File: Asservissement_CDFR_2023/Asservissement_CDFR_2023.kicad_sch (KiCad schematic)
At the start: 127 parts, among them IC1 A3930KJPTR-T, IC2 A3930KJPTR-T, J1 Connecteur batterie, J10 Free Connecteur, J11 Conn_01x02, J12 Conn_01x02, J13 Connecteur Odométrie, J2 Conn_01x03, J3 Conn_01x05, J4 Connecteur Programmation, J5 Conn_01x03, J6 Connecteur Odométrie, J7 Conn_01x03, J8 Conn_01x03, J9 Conn_01x05, Q1 QM6006D, Q10 QM6006D, Q11 QM6006D, Q12 QM6006D, Q13 Q_NMOS_GDS, Q2 QM6006D, Q3 QM6006D, Q4 QM6006D, Q5 QM6006D, Q6 QM6006D, Q7 QM6006D, Q8 QM6006D, Q9 QM6006D, U1 LM317_SOT-223, U3 STM32F401RCTx, U4 LMR16020PDDA, Y1 Crystal_GND24

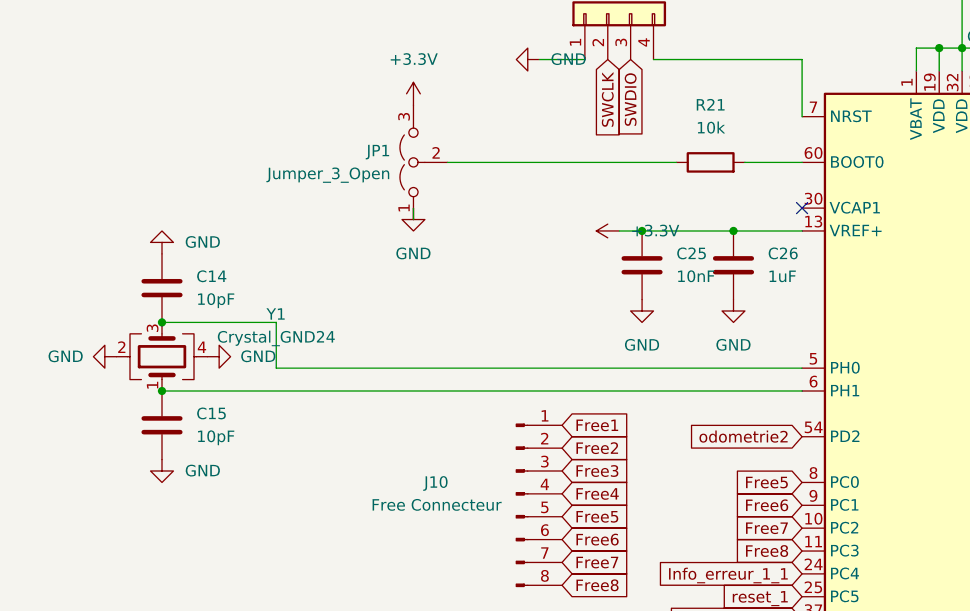
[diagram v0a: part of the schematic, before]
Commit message: add resistor for the crystal, add capacitor to Vcap, add logo and text for the voltage tolerance
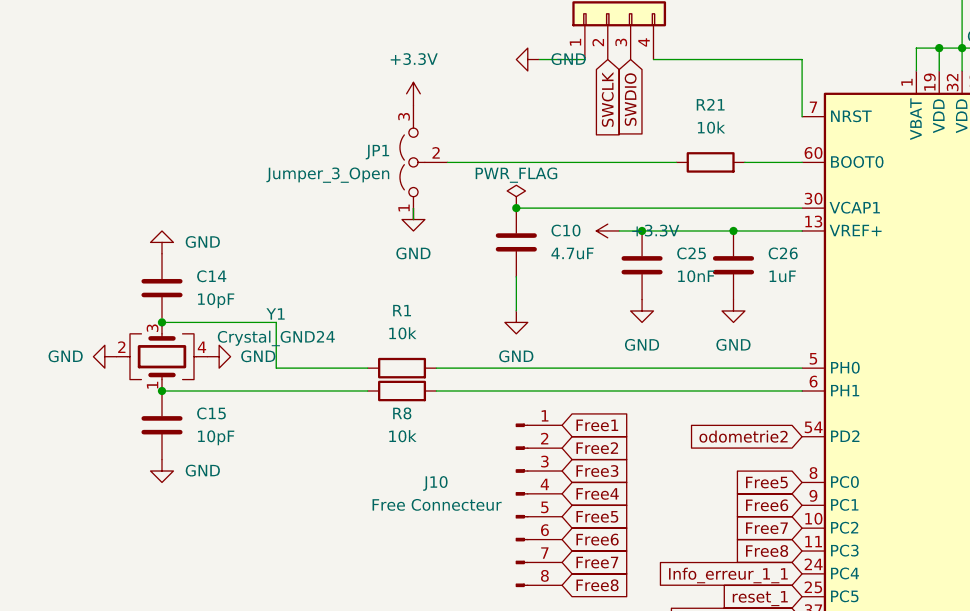
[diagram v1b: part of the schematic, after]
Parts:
- added C10: 4.7uF, Capacitor_SMD:C_0805_2012Metric_Pad1.18x1.45mm_HandSolder, symbol Device:C
- added R1, R8: 10k, Resistor_SMD:R_0805_2012Metric_Pad1.20x1.40mm_HandSolder, symbol Device:R
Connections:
- net GND: now also C10.2
- net at C14.2, Y1.3: now also R1.1; no longer U3.5 (PH0)
- net at U3.30 (VCAP1): now also C10.1
- net at C15.1, Y1.1: now also R8.1; no longer U3.6 (PH1)
- new net: R1.2, U3.5 (PH0)
- new net: R8.2, U3.6 (PH1)
- no-connect marks 14 -> 13
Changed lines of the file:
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@@
   (junction (at 506.73 44.45) (diameter 0) (color 0 0 0 0)
   )
+  (junction (at 92.71 200.66) (diameter 0) (color 0 0 0 0)
+  )
   (junction (at 436.88 92.71) (diameter 0) (color 0 0 0 0)
   )
@@
   (no_connect (at 398.78 241.3))
   (no_connect (at 401.32 241.3))
-  (no_connect (at 124.46 200.66))
   (no_connect (at 388.62 259.08))
   (wire (pts (xy 506.73 69.85) (xy 506.73 82.55))
@@
     (stroke (width 0) (type default) (color 0 0 0 0))
   )
-  (wire (pts (xy 124.46 220.98) (xy 53.34 220.98))
+  (wire (pts (xy 124.46 220.98) (xy 83.82 220.98))
     (stroke (width 0) (type default) (color 0 0 0 0))
   )
@@
     (stroke (width 0) (type default) (color 0 0 0 0))
   )
-  (wire (pts (xy 66.04 218.44) (xy 124.46 218.44))
+  (wire (pts (xy 66.04 218.44) (xy 76.2 218.44))
     (stroke (width 0) (type default) (color 0 0 0 0))
   )
@@
     (stroke (width 0) (type default) (color 0 0 0 0))
   )
+  (wire (pts (xy 92.71 208.28) (xy 92.71 212.09))
+    (stroke (width 0) (type default) (color 0 0 0 0))
+  )
   (wire (pts (xy 53.34 213.36) (xy 66.04 213.36))
     (stroke (width 0) (type default) (color 0 0 0 0))
@@
     (stroke (width 0) (type default) (color 0 0 0 0))
   )
+  (wire (pts (xy 83.82 218.44) (xy 124.46 218.44))
+    (stroke (width 0) (type default) (color 0 0 0 0))
+  )
   (wire (pts (xy 544.83 110.49) (xy 544.83 107.95))
     (stroke (width 0) (type default) (color 0 0 0 0))
@@
     (stroke (width 0) (type default) (color 0 0 0 0))
   )
+  (wire (pts (xy 76.2 220.98) (xy 53.34 220.98))
+    (stroke (width 0) (type default) (color 0 0 0 0))
+  )
   (wire (pts (xy 434.34 284.48) (xy 453.39 284.48))
     (stroke (width 0) (type default) (color 0 0 0 0))
@@
     (stroke (width 0) (type default) (color 0 0 0 0))
   )
+  (wire (pts (xy 92.71 200.66) (xy 124.46 200.66))
+    (stroke (width 0) (type default) (color 0 0 0 0))
+  )
   (wire (pts (xy 147.32 52.07) (xy 147.32 64.77))
     (stroke (width 0) (type default) (color 0 0 0 0))
@@
     (pin "3")
   )
+  (symbol (lib_id "Device:R") (at 80.01 220.98 90) (unit 1)
+    (in_bom yes) (on_board yes)
+    (property "Reference" "R8" (id 0) (at 80.01 223.52 90))
+    (property "Value" "10k" (id 1) (at 80.01 226.06 90))
+    (property "Footprint" "Resistor_SMD:R_0805_2012Metric_Pad1.20x1.40mm_HandSolder" (id 2) (at 80.01 222.758 90)
+      (effects (font (size 1.27 1.27)) hide)
+    )
+    (property "Datasheet" "~" (id 3) (at 80.01 220.98 0)
+      (effects (font (size 1.27 1.27)) hide)
+    )
+    (pin "1")
+    (pin "2")
+  )
   (symbol (lib_id "power:GND") (at 58.42 217.17 90) (unit 1)
     (in_bom yes) (on_board yes)
@@
     (pin "2")
   )
+  (symbol (lib_id "power:GND") (at 92.71 212.09 0) (unit 1)
+    (in_bom yes) (on_board yes) (fields_autoplaced)
+    (property "Reference" "#PWR0109" (id 0) (at 92.71 218.44 0)
+      (effects (font (size 1.27 1.27)) hide)
+    )
+    (property "Value" "GND" (id 1) (at 92.71 217.17 0))
+    (property "Footprint" "" (id 2) (at 92.71 212.09 0)
+      (effects (font (size 1.27 1.27)) hide)
+    )
+    (property "Datasheet" "" (id 3) (at 92.71 212.09 0)
+      (effects (font (size 1.27 1.27)) hide)
+    )
+    (pin "1")
+  )
   (symbol (lib_id "power:GND") (at 196.85 228.6 90) (unit 1)
     (in_bom yes) (on_board yes) (fields_autoplaced)
@@
     (pin "2")
   )
+  (symbol (lib_id "Device:C") (at 92.71 204.47 0) (unit 1)
+    (in_bom yes) (on_board yes) (fields_autoplaced)
+    (property "Reference" "C10" (id 0) (at 96.52 203.1999 0)
+      (effects (font (size 1.27 1.27)) (justify left))
+    )
+    (property "Value" "4.7uF" (id 1) (at 96.52 205.7399 0)
+      (effects (font (size 1.27 1.27)) (justify left))
+    )
+    (property "Footprint" "Capacitor_SMD:C_0805_2012Metric_Pad1.18x1.45mm_HandSolder" (id 2) (at 93.6752 208.28 0)
+      (effects (font (size 1.27 1.27)) hide)
+    )
+    (property "Datasheet" "~" (id 3) (at 92.71 204.47 0)
+      (effects (font (size 1.27 1.27)) hide)
+    )
+    (pin "1")
+    (pin "2")
+  )
   (symbol (lib_id "power:+3.3V") (at 142.24 161.29 0) (unit 1)
     (in_bom yes) (on_board yes) (fields_autoplaced)
@@
     (pin "1")
   )
+  (symbol (lib_id "Device:R") (at 80.01 218.44 90) (unit 1)
+    (in_bom yes) (on_board yes) (fields_autoplaced)
+    (property "Reference" "R1" (id 0) (at 80.01 212.09 90))
+    (property "Value" "10k" (id 1) (at 80.01 214.63 90))
+    (property "Footprint" "Resistor_SMD:R_0805_2012Metric_Pad1.20x1.40mm_HandSolder" (id 2) (at 80.01 220.218 90)
+      (effects (font (size 1.27 1.27)) hide)
+    )
+    (property "Datasheet" "~" (id 3) (at 80.01 218.44 0)
+      (effects (font (size 1.27 1.27)) hide)
+    )
+    (pin "1")
+    (pin "2")
+  )
   (symbol (lib_id "power:GND") (at 408.94 143.51 0) (unit 1)
     (in_bom yes) (on_board yes) (fields_autoplaced)
@@
     (pin "1")
   )
+  (symbol (lib_id "power:PWR_FLAG") (at 92.71 200.66 0) (unit 1)
+    (in_bom yes) (on_board yes)
+    (property "Reference" "#FLG0102" (id 0) (at 92.71 198.755 0)
+      (effects (font (size 1.27 1.27)) hide)
+    )
+    (property "Value" "PWR_FLAG" (id 1) (at 92.71 196.85 0))
+    (property "Footprint" "" (id 2) (at 92.71 200.66 0)
+      (effects (font (size 1.27 1.27)) hide)
+    )
+    (property "Datasheet" "~" (id 3) (at 92.71 200.66 0)
+      (effects (font (size 1.27 1.27)) hide)
+    )
+    (pin "1")
+  )
   (symbol (lib_id "Device:R") (at 468.63 121.92 0) (unit 1)
     (in_bom yes) (on_board yes)
@@
       (reference "#FLG0101") (unit 1) (value "PWR_FLAG") (footprint "")
     )
+    (path "/d5fc98bd-8b4a-41f7-8f4d-cab165222fda"
+      (reference "#FLG0102") (unit 1) (value "PWR_FLAG") (footprint "")
+    )
     (path "/c2ed825f-7bd1-4467-a5ef-8700f9ccf66f"
       (reference "#FLG0104") (unit 1) (value "PWR_FLAG") (footprint "")
@@
       (reference "#PWR0108") (unit 1) (value "+5V") (footprint "")
     )
+    (path "/9d1bcaca-cd1d-4150-9486-f84ed021b7ad"
+      (reference "#PWR0109") (unit 1) (value "GND") (footprint "")
+    )
     (path "/cb70175c-97c6-48d6-a02b-93d4e11b3d49"
       (reference "C1") (unit 1) (value "470nF") (footprint "Capacitor_SMD:C_0805_2012Metric_Pad1.18x1.45mm_HandSolder")
@@
       (reference "C9") (unit 1) (value "47nF") (footprint "Capacitor_SMD:C_0805_2012Metric_Pad1.18x1.45mm_HandSolder")
     )
+    (path "/aa656297-d170-45c0-9433-050e813c7e2b"
+      (reference "C10") (unit 1) (value "4.7uF") (footprint "Capacitor_SMD:C_0805_2012Metric_Pad1.18x1.45mm_HandSolder")
+    )
     (path "/3229e465-658c-497b-aa13-bb46a30754bf"
       (reference "C11") (unit 1) (value "100uF") (footprint "Capacitor_SMD:CP_Elec_10x10.5")
@@
       (reference "Q13") (unit 1) (value "Q_NMOS_GDS") (footprint "Package_TO_SOT_SMD:TO-252-2")
     )
+    (path "/bf57164e-1c8b-4348-9c0e-1bd3168f94fd"
+      (reference "R1") (unit 1) (value "10k") (footprint "Resistor_SMD:R_0805_2012Metric_Pad1.20x1.40mm_HandSolder")
+    )
     (path "/cf693dd7-8b45-433c-b7b1-3d9bff0f41a1"
       (reference "R2") (unit 1) (value "2k4") (footprint "Resistor_SMD:R_0805_2012Metric_Pad1.20x1.40mm_HandSolder")
@@
       (reference "R7") (unit 1) (value "560") (footprint "Resistor_SMD:R_0805_2012Metric_Pad1.20x1.40mm_HandSolder")
     )
+    (path "/56846ada-828b-42f8-a2c3-f017ddfc46d7"
+      (reference "R8") (unit 1) (value "10k") (footprint "Resistor_SMD:R_0805_2012Metric_Pad1.20x1.40mm_HandSolder")
+    )
     (path "/5cb72c38-3e9e-44d9-be58-abf36ec7a07c"

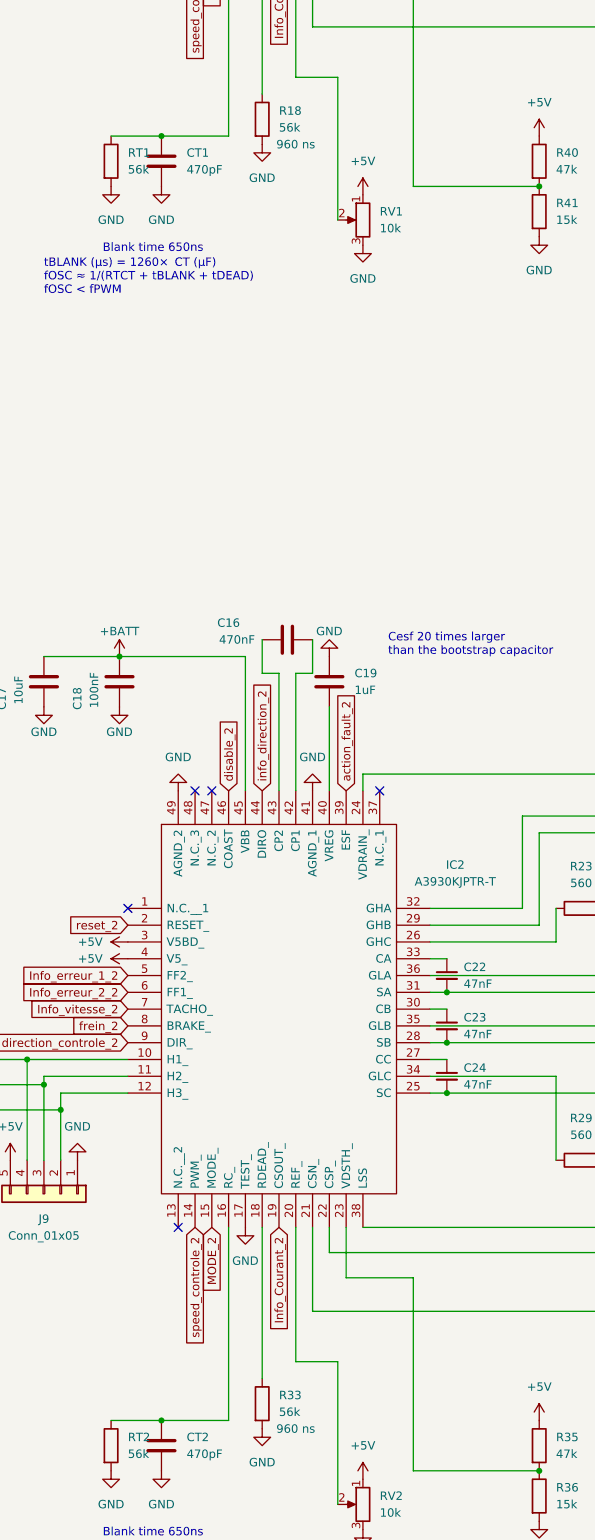
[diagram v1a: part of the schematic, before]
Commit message: change one resistor
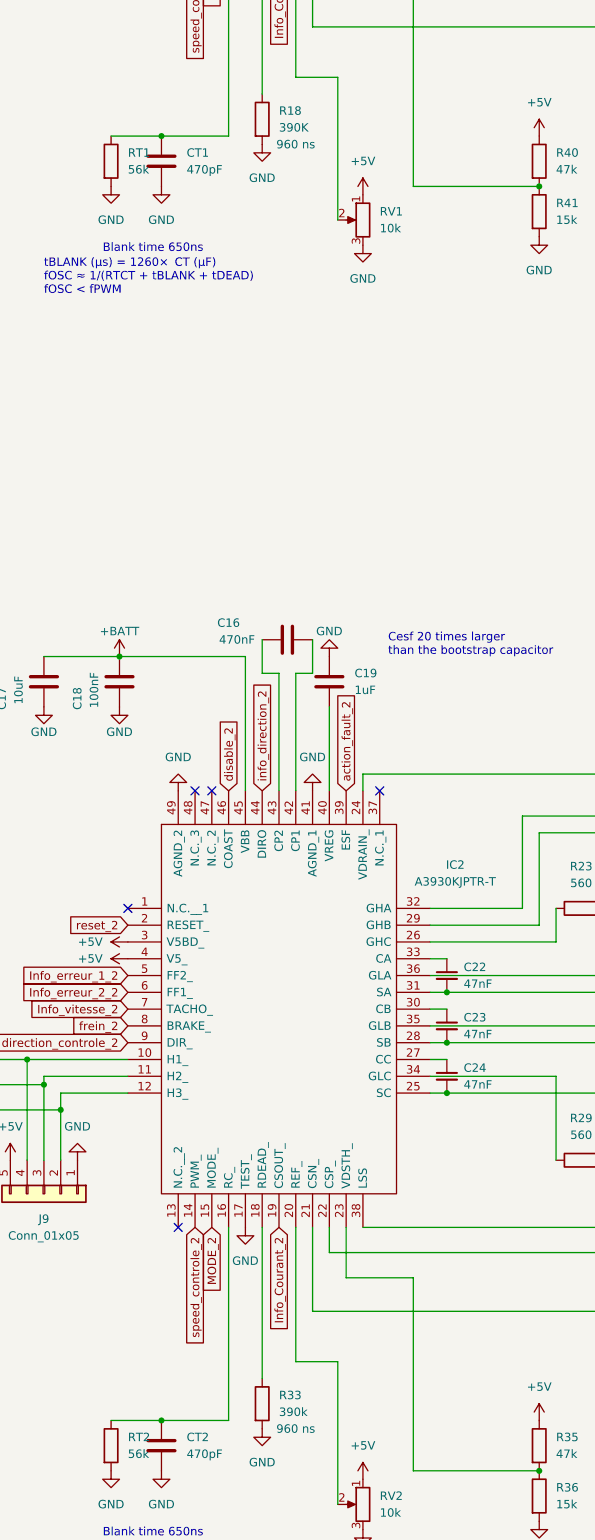
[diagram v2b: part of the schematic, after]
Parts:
- R18: value 56k -> 390K
- R33: value 56k -> 390k
- R43, R44: footprint Resistor_SMD:R_0805_2012Metric -> Resistor_SMD:R_0805_2012Metric_Pad1.20x1.40mm_HandSolder
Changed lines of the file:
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@@
       (effects (font (size 1.27 1.27)) (justify left))
     )
-    (property "Footprint" "Resistor_SMD:R_0805_2012Metric" (id 2) (at 145.542 48.26 90)
+    (property "Footprint" "Resistor_SMD:R_0805_2012Metric_Pad1.20x1.40mm_HandSolder" (id 2) (at 145.542 48.26 90)
       (effects (font (size 1.27 1.27)) hide)
     )
@@
       (effects (font (size 1.27 1.27)) (justify left))
     )
-    (property "Value" "56k" (id 1) (at 411.48 335.2799 0)
+    (property "Value" "390k" (id 1) (at 411.48 335.2799 0)
       (effects (font (size 1.27 1.27)) (justify left))
     )
@@
       (effects (font (size 1.27 1.27)) (justify left))
     )
-    (property "Value" "56k" (id 1) (at 411.48 140.9699 0)
+    (property "Value" "390K" (id 1) (at 411.48 140.9699 0)
       (effects (font (size 1.27 1.27)) (justify left))
     )
@@
       (effects (font (size 1.27 1.27)) (justify left))
     )
-    (property "Footprint" "Resistor_SMD:R_0805_2012Metric" (id 2) (at 145.542 40.64 90)
+    (property "Footprint" "Resistor_SMD:R_0805_2012Metric_Pad1.20x1.40mm_HandSolder" (id 2) (at 145.542 40.64 90)
       (effects (font (size 1.27 1.27)) hide)
     )
@@
     )
     (path "/6c4fef66-2619-4860-9b7a-7ef2c0d513f7"
-      (reference "R18") (unit 1) (value "56k") (footprint "Resistor_SMD:R_0805_2012Metric_Pad1.20x1.40mm_HandSolder")
+      (reference "R18") (unit 1) (value "390K") (footprint "Resistor_SMD:R_0805_2012Metric_Pad1.20x1.40mm_HandSolder")
     )
     (path "/aa5702bb-f608-4e2a-aea8-d22c4c59b90c"
@@
     )
     (path "/54801370-0589-40df-9d8b-2689fd0b6c09"
-      (reference "R33") (unit 1) (value "56k") (footprint "Resistor_SMD:R_0805_2012Metric_Pad1.20x1.40mm_HandSolder")
+      (reference "R33") (unit 1) (value "390k") (footprint "Resistor_SMD:R_0805_2012Metric_Pad1.20x1.40mm_HandSolder")
     )
     (path "/2825674f-e023-4940-bd92-18e379cca829"
@@
     )
     (path "/8c2258c2-4bc5-4a88-b138-75c29a1b0fe5"
-      (reference "R43") (unit 1) (value "56k") (footprint "Resistor_SMD:R_0805_2012Metric")
+      (reference "R43") (unit 1) (value "56k") (footprint "Resistor_SMD:R_0805_2012Metric_Pad1.20x1.40mm_HandSolder")
     )
     (path "/4c1d1137-9b5a-40bb-ad66-108c1af250cf"
-      (reference "R44") (unit 1) (value "10k") (footprint "Resistor_SMD:R_0805_2012Metric")
+      (reference "R44") (unit 1) (value "10k") (footprint "Resistor_SMD:R_0805_2012Metric_Pad1.20x1.40mm_HandSolder")
     )
     (path "/3f3742ef-b9df-4d47-888e-7cfef46889d2"
